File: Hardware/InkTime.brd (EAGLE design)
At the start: 46 x 35 mm, 105 parts, among them IC1 BQ25180YBGR_BQ25180YBGRBBQ, IC2 DRV2605YZFR, IC3 BMA421, IC9 RT6160AWSC, J1 503480-2400, J2 TC2030-IDC, J4 KH-TYPE-C-16P, Q1 ESP32_C6_LIBRARY_4_ESP32_WROV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, Q3 SI1308EDL-T1-GE3, U3 MAX17048G+T10, X1 32MHz, X2 32.768kHz

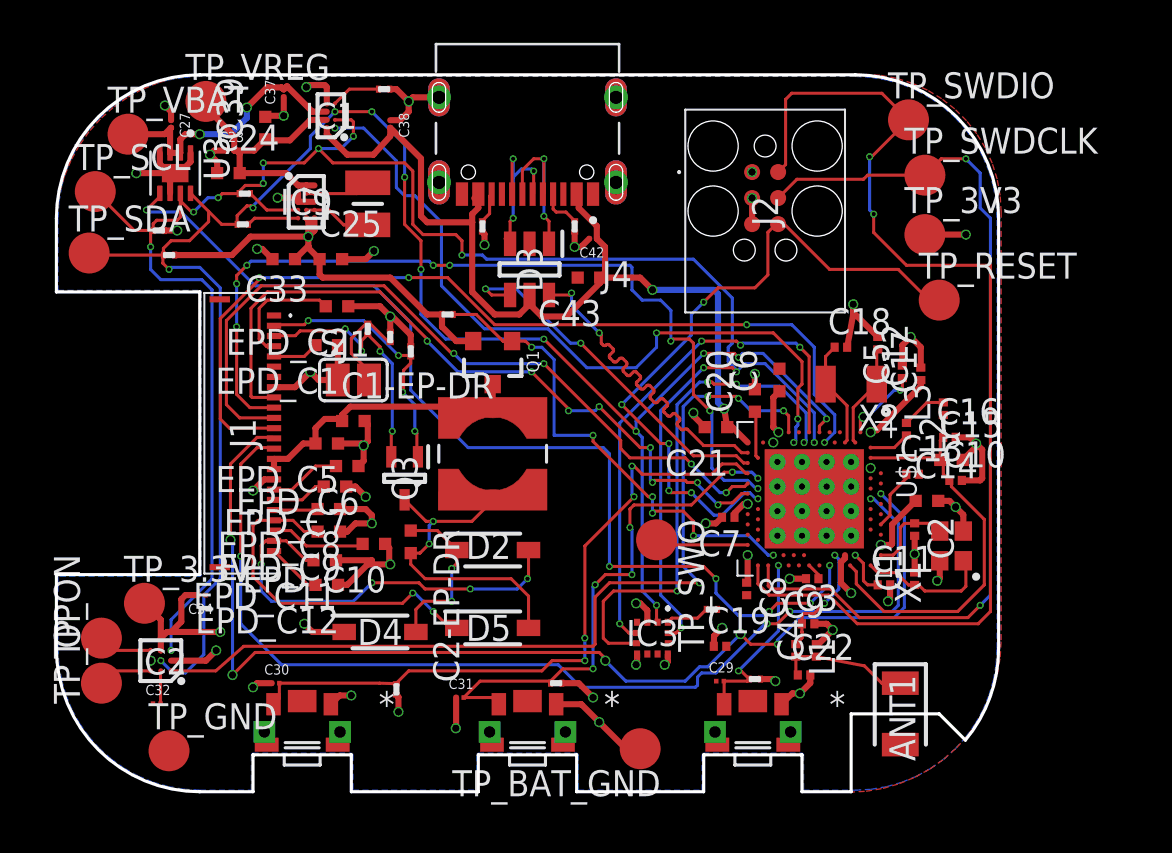
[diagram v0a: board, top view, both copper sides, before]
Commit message: Add PCB with silkscreen layer
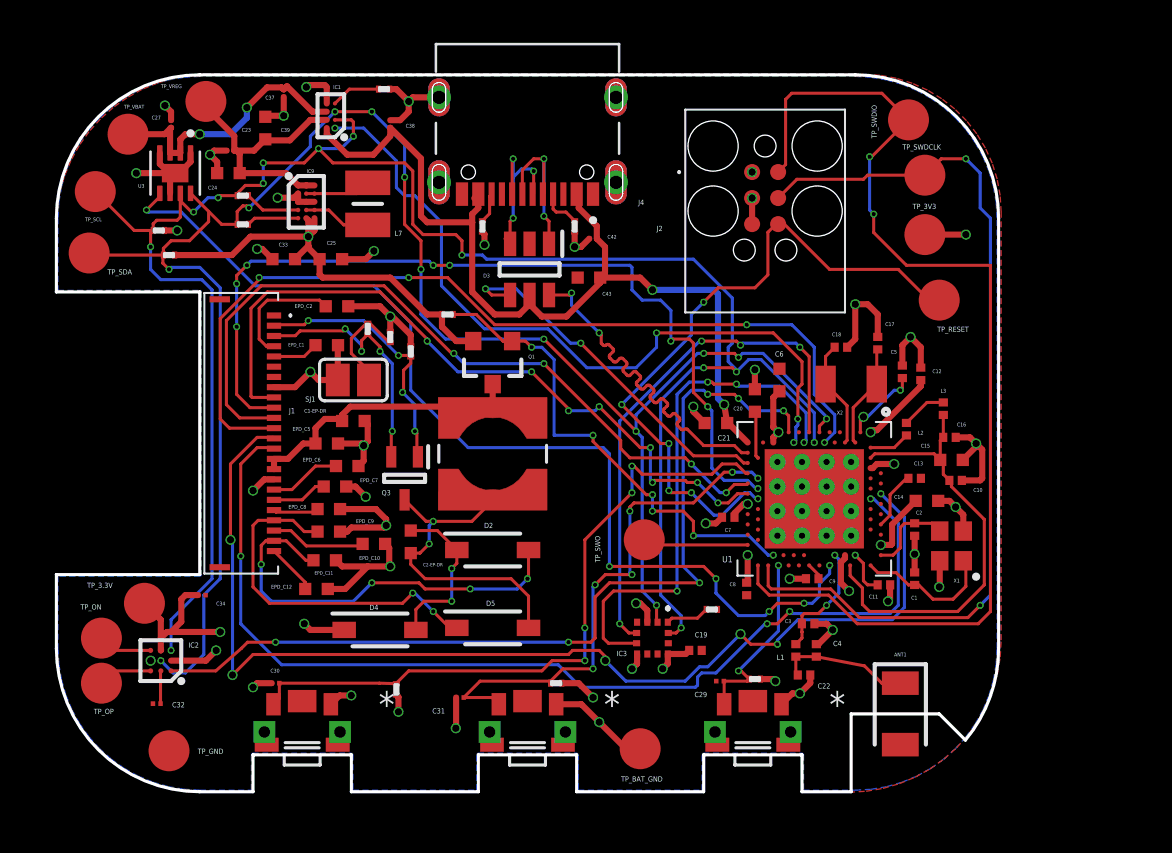
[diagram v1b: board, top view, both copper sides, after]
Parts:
- moved C19 1.22 mm to (8.20, -10.6)
- moved TP_SWO 0.60 mm to (5.70, -5.20)
- moved EPD_C12 0.54 mm to (-10.3, -7.60)
- moved C13 0.22 mm to (18.9, -2.20)
- moved C21 0.20 mm to (9.20, 0.50)
- moved R4 0.14 mm to (-13.9, 11.6)
- moved D4 0.10 mm to (-7.20, -9.60)
- renumbered U$1 to U1
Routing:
- net GND: track 93.7 -> 97.4 mm
- net 3V3: track 50.4 -> 51.6 mm, vias 18 -> 16
- net SWO: track 4.55 -> 5.15 mm
- net N$12: track 21.1 -> 21.6 mm
- net HAPTIC_EN: track 44.4 -> 44.7 mm, vias 4 -> 6

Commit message: Fixed minor schematic and board issues
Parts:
- Q1: value ESP32_C6_LIBRARY_4_ESP32_WROVER_SPARKFUN-DISCRETESEMI_MOSFET_PCH -> DMG2305UX-7
- moved L7 0.50 mm to (-8.30, 11.2)
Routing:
- net GND: track 97.4 -> 98.4 mm
- net PMIC_INT: track 36.0 -> 36.6 mm
- net 3V3: track 51.6 -> 52.2 mm
- net LX2: track 3.30 -> 2.80 mm
- net LX1: track 3.22 -> 2.72 mm
